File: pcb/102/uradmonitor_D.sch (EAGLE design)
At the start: 93 parts, among them IC2 MEGA128-A, IC4 TP4056, IC5 BME280, Q1 8Mhz, T1 MMBT2907, T2 MPSA42, T3 MMBT2222, T4 2907, T5 MMBT2907, T7 MMBT2222, U1 FT232RLSSOP, U2 LTC3440

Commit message: revision pcb 102. revision enclosure 103
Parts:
- removed JP1: (no value), adafruit:PINHD-1X3
- removed LCD1: TJCTM24024-SPI2.4", uradmonitor:TJCTM24024-SPI2.4"
- removed U$1: TJCTM24024-PCBCON, uradmonitor:TJCTM24024-PCBCON
- removed U$3: 10uH, digital-toy:INDUCTOR1206H*
- removed U$4: 2.2mH, digital-toy:INDUCTOR1206H*
- added C22, C23: 10uF, resistor:C-EUC0805
- added JP2, JP3, JP4: (no value), adafruit:PINHD-1X1CB
- added L1: 10uH, uradmonitor:INDUCTOR
- added L2: 2.2mH, uradmonitor:INDUCTOR
- added R36: 100K, rcl:R-EU_R0805
- added R37: 3R9, resistor:R-EU_R0805
- added R38: 10M 1%, rcl:R-EU_0204/7
- added U$8: 65Z5, uradmonitor:65Z5
- added U3: AT24C256C, Atmel_By_element14_Batch_1-00:AT24C512BN-SH25-B
- added U4: DS1337S+, Maxim_By_element14_Batch_1:DS1337S+
- added X1, X2: (no value), adafruit:XTAL-3.2X1.5
- C1, C2: value 33p -> 22pF
- C14, C19, C20: device rcl:C-EU050-025X075 -> rcl:C-EUC1206K
- Q1: value 8Mhz -> (none); device special:XTAL/S -> adafruit:XTAL-4-3225
- Q2: value (none) -> SI2305; device adafruit:CRYSTALTC26H -> uradmonitor:SI2305
- R16: value 47K 1% -> 100K 1%
- SENSOR2: value SENSOR_GY68GY-86DIP -> BMP180
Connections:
- removed net N$25: BATTERY1.VCC, C10.2, IC4.BAT, JP1.1, R25.2, S2.2, U2.VIN
- removed net N$48: R28.2, S2.1
- removed net N$58: C20.1, D4.C, R15.2, R17.1
- new net ALARM_CONTROL: Q2.D, R28.2, S2.1
- new net N$35: C14.1, C20.1, D2.C, D3.A
- new net N$54: C20.2, D4.C, R15.2, R17.1
- new net N$55: U4.X2, X2.P$1
- new net N$61: R15.1, R38.2
- new net N$65: Q2.G, R36.1, U4.~INTA
- new net N$69: C1.1, Q1.G1
- new net N$75: R37.2, U$6.VCC_LED
- new net VBAT: BATTERY1.VCC, C10.2, IC4.BAT, JP2.1, Q2.S, R25.2, R36.2, S2.2, SP4.+, U2.VIN, U4.VCC
- net GND: now also C22.2, C23.2, JP4.1, Q1.G2, U$6.GND_1, U$6.GND_11, U$6.GND_12, U$6.GND_13, U$6.GND_14, U$6.GND_8, U$8.GND, U3.A0, U3.A1, U3.A2, U3.GND, U3.WP, U4.GND; no longer C1.1, C20.2, JP1.3, U$1.GND
- net MCU_HV_ADC: now also R38.1; no longer R15.1
- net MCU_SCL: now also U3.SCL, U4.SCL
- net MCU_SDA: now also U3.SDA, U4.SDA
- net N$10: now also L1.P$1; no longer U$3.1
- net N$11: now also Q1.X2; no longer Q1.1
- net N$12: now also X1.P$2; no longer Q2.1
- net N$13: now also R37.1; no longer U$1.LED
- net N$14: now also U$6.SDI(>MOSI); no longer U$1.SDI
- net N$30: now also X1.P$1; no longer Q2.2
- net N$31: now also JP3.1; no longer JP1.2
- net N$36: now also U$6.RESET; no longer U$1.RESET
- net N$38: now also U$6.D/C; no longer U$1.D/C
- net N$39: now also U$6.CS; no longer U$1.CS
- net N$4: now also L1.P$2; no longer U$3.2
- net N$40: now also U$6.XP; no longer U$1.TOUCH_XP
- net N$41: now also U$6.YN; no longer U$1.TOUCH_YN
- net N$51: now also L2.P$2; no longer U$4.2
- net N$52: now also C22.1, U$6.VCC, U$8.VO; no longer U$6.GND_1, U$6.GND_11, U$6.GND_12, U$6.GND_13, U$6.GND_14, U$6.GND_8
- net N$56: now also U4.X1, X2.P$2; no longer C14.1, D2.C, D3.A
- net N$6: now also U$6.SCK; no longer U$1.SCK
- net N$9: now also Q1.X1; no longer Q1.2
- net VCC_3.3V: now also C23.1, L2.P$1, U$8.+VIN, U3.VCC; no longer SP4.+, U$1.VCC, U$4.1
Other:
- moved on the sheet: BATTERY1, C10, C11, C14, C19, C20, C3, C4, C5, C9, D2, D4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

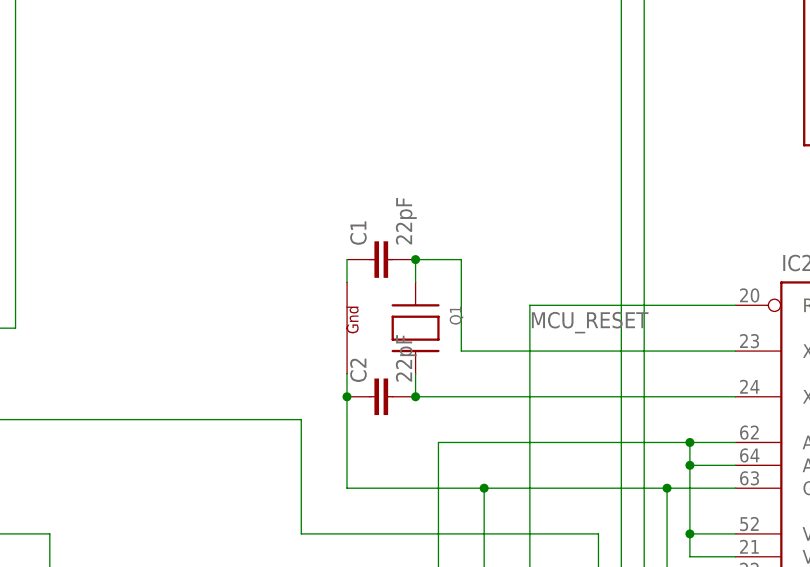
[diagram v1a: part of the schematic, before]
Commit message: 12pF caps to 16MHz crystal
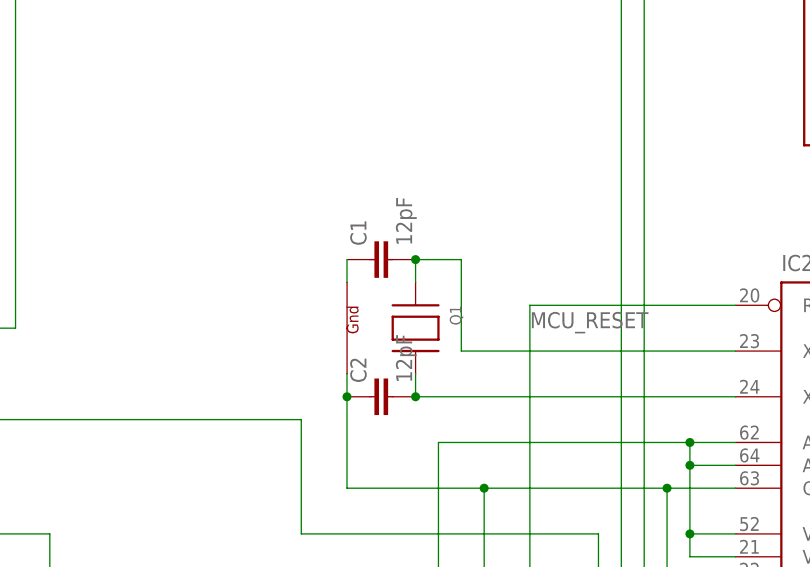
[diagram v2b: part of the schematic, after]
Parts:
- C1, C2: value 22pF -> 12pF
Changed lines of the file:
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@@
 <setting verticaltext="up"/>
 </settings>
-<grid distance="0.05" unitdist="inch" unit="inch" style="lines" multiple="1" display="no" altdistance="0.01" altunitdist="inch" altunit="inch"/>
+<grid distance="0.1" unitdist="inch" unit="inch" style="lines" multiple="1" display="no" altdistance="0.01" altunitdist="inch" altunit="inch"/>
 <layers>
 <layer number="1" name="Top" color="4" fill="1" visible="no" active="no"/>
@@
 <part name="FRAME1" library="frames" deviceset="DINA3_L" device=""/>
 <part name="J$1" library="sparkfun-connectors" deviceset="SMA_EDGE" device=""/>
-<part name="C1" library="rcl" deviceset="C-EU" device="C0805K" value="22pF"/>
-<part name="C2" library="rcl" deviceset="C-EU" device="C0805K" value="22pF"/>
+<part name="C1" library="rcl" deviceset="C-EU" device="C0805K" value="12pF"/>
+<part name="C2" library="rcl" deviceset="C-EU" device="C0805K" value="12pF"/>
 <part name="C4" library="rcl" deviceset="C-EU" device="C0805K" value="100nF"/>
 <part name="C5" library="rcl" deviceset="C-EU" device="C0805K" value="100nF"/>
